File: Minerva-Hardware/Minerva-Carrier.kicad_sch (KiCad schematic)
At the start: 16 parts, among them J11 USB_C_Receptacle_USB2.0, Q2 RQ6E080AJ, U1 BQ25798

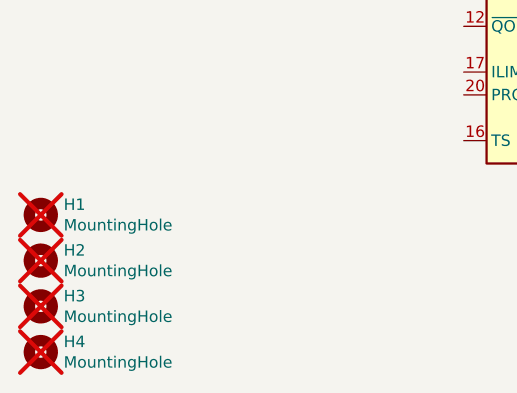
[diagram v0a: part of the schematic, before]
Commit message: Rename and commit actions due to mishap of location naming/saving
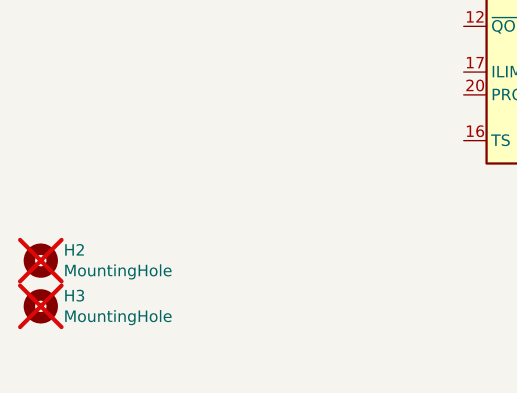
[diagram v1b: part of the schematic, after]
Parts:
- removed H1, H4: MountingHole, CM5IO:MountingHole_2.7mm_M2.5_DIN965, symbol Mechanical:MountingHole

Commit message: renames
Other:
- moved on the sheet: D4, R2
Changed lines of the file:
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@@
 	(wire
 		(pts
-			(xy 227.33 127) (xy 231.14 127)
+			(xy 144.78 168.91) (xy 148.59 168.91)
 		)
 		(stroke
@@
 	(wire
 		(pts
-			(xy 245.11 127) (xy 245.11 128.27)
+			(xy 162.56 168.91) (xy 162.56 170.18)
 		)
 		(stroke
@@
 	(wire
 		(pts
+			(xy 139.7 168.91) (xy 135.89 168.91)
+		)
+		(stroke
+			(width 0)
+			(type default)
+		)
+	)
+	(wire
+		(pts
 			(xy 72.39 80.01) (xy 83.82 80.01)
 		)
@@
 	(wire
 		(pts
-			(xy 238.76 127) (xy 245.11 127)
+			(xy 156.21 168.91) (xy 162.56 168.91)
 		)
 		(stroke
@@
 	)
 	(label "CHARGE_IND_SIG"
-		(at 222.25 127 180)
+		(at 135.89 168.91 180)
 		(effects
 			(font
@@
 	(symbol
 		(lib_id "Device:R_Small_US")
-		(at 224.79 127 90)
+		(at 142.24 168.91 90)
 		(unit 1)
 		(exclude_from_sim no)
@@
 		(fields_autoplaced yes)
 		(property "Reference" "R2"
-			(at 224.79 120.65 90)
+			(at 142.24 162.56 90)
 			(effects
 				(font
@@
 		)
 		(property "Value" "10k"
-			(at 224.79 123.19 90)
+			(at 142.24 165.1 90)
 			(effects
 				(font
@@
 		)
 		(property "Footprint" "Resistor_SMD:R_0201_0603Metric"
-			(at 224.79 127 0)
+			(at 142.24 168.91 0)
 			(effects
 				(font
@@
 		)
 		(property "Datasheet" "~"
-			(at 224.79 127 0)
+			(at 142.24 168.91 0)
 			(effects
 				(font
@@
 		)
 		(property "Description" "Resistor, small US symbol"
-			(at 224.79 127 0)
+			(at 142.24 168.91 0)
 			(effects
 				(font
@@
 	(symbol
 		(lib_id "Device:LED")
-		(at 234.95 127 180)
+		(at 152.4 168.91 180)
 		(unit 1)
 		(exclude_from_sim no)
@@
 		(fields_autoplaced yes)
 		(property "Reference" "D4"
-			(at 236.5375 119.38 0)
+			(at 153.9875 161.29 0)
 			(effects
 				(font
@@
 		)
 		(property "Value" "LED"
-			(at 236.5375 121.92 0)
+			(at 153.9875 163.83 0)
 			(effects
 				(font
@@
 		)
 		(property "Footprint" "LED_SMD:LED_0201_0603Metric"
-			(at 234.95 127 0)
+			(at 152.4 168.91 0)
 			(effects
 				(font
@@
 		)
 		(property "Datasheet" "~"
-			(at 234.95 127 0)
+			(at 152.4 168.91 0)
 			(effects
 				(font
@@
 		)
 		(property "Description" "Light emitting diode"
-			(at 234.95 127 0)
+			(at 152.4 168.91 0)
 			(effects
 				(font
@@
 		)
 		(property "Sim.Pins" "1=K 2=A"
-			(at 234.95 127 0)
+			(at 152.4 168.91 0)
 			(effects
 				(font
@@
 	(symbol
 		(lib_id "power:GND")
-		(at 245.11 128.27 0)
+		(at 162.56 170.18 0)
 		(unit 1)
 		(exclude_from_sim no)
@@
 		(fields_autoplaced yes)
 		(property "Reference" "#PWR04"
-			(at 245.11 134.62 0)
+			(at 162.56 176.53 0)
 			(effects
 				(font
@@
 		)
 		(property "Value" "GND"
-			(at 245.11 133.35 0)
+			(at 162.56 175.26 0)
 			(effects
 				(font
@@
 		)
 		(property "Footprint" ""
-			(at 245.11 128.27 0)
+			(at 162.56 170.18 0)
 			(effects
 				(font
@@
 		)
 		(property "Datasheet" ""
-			(at 245.11 128.27 0)
+			(at 162.56 170.18 0)
 			(effects
 				(font
@@
 		)
 		(property "Description" "Power symbol creates a global label with name \"GND\" , ground"
-			(at 245.11 128.27 0)
+			(at 162.56 170.18 0)
 			(effects
 				(font
@@
 		)
 		(instances
-			(project "CM5IO"
+			(project "Minerva-Carrier"
 				(path "/e63e39d7-6ac0-4ffd-8aa3-1841a4541b55"
 					(page "3")
@@
 		)
 		(instances
-			(project "CM5IO"
+			(project "Minerva-Carrier"
 				(path "/e63e39d7-6ac0-4ffd-8aa3-1841a4541b55"
 					(page "2")
@@
 		)
 		(instances
-			(project "CM5IO"
+			(project "Minerva-Carrier"
 				(path "/e63e39d7-6ac0-4ffd-8aa3-1841a4541b55"
 					(page "4")
